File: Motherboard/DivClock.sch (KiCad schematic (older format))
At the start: 33 parts

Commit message: More work on Motherboard
Began work on PCB Routing
Began work on DMA
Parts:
- removed U?: 74AHC1G14, symbol 74xGxx:74AHC1G14
- added U13: 74LS14, symbol 74xx:74LS14
- added unit 7 of U16
- added U17: 74LS32, Housings_DIP:DIP-14_W7.62mm_Socket, symbol 74xx:74LS32
- added unit 5 of U18
- added unit 5 of U20
- added U21: 40106, Housings_DIP:DIP-40_W15.24mm_Socket, symbol 4xxx:40106
- R3, R4: renamed from R?; footprint (none) -> Resistors_THT:R_Axial_DIN0204_L3.6mm_D1.6mm_P5.08mm_Horizontal
- SW1: renamed from SW?; value SW_SPST -> TURBO; footprint (none) -> Pin_Headers:Pin_Header_Straight_1x02_Pitch2.00mm
- SW2: renamed from SW?; value SW_SPST -> FREEZE; footprint (none) -> Pin_Headers:Pin_Header_Straight_1x02_Pitch2.00mm
- U10, U11, U16, U18, U19, U20, U8, U9: renamed from U?; footprint (none) -> Housings_DIP:DIP-14_W7.62mm_Socket
- gave numbers to parts that had none: 11
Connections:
- wire segments 122 -> 128
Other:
- moved on the sheet: R3, R4

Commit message: Large sync
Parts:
- removed unit 1 of U18
- removed unit 1 of U20
- added unit 1 of U10
- U13: footprint (none) -> Housings_DIP:DIP-14_W7.62mm_Socket
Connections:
- net SYS_CLK: now also U19.9 (Q)
- net at U15.4 (Za), U16.3, U19.3 (C): now also U19.11 (C)
- net at U19.2 (D): now also U10.3; no longer U19.6 (~Q)
- net at U19.5 (Q): now also U19.12 (D); no longer U19.11 (C)
- net at U19.8 (~Q): now also U10.2; no longer U19.12 (D)
- new net: U10.1, U19.6 (~Q)
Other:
- moved on the sheet: U19B
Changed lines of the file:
@@
 L 74xx:74HC74 U19
 U 2 1 5BFDC06F
-P 8775 1225
-F 0 "U19" H 8925 1525 50  0000 C CNN
-F 1 "74HC74" H 9075 930 50  0000 C CNN
-F 2 "Housings_DIP:DIP-14_W7.62mm_Socket" H 8775 1225 50  0001 C CNN
-F 3 "" H 8775 1225 50  0001 C CNN
-	2    8775 1225
-	1    0    0    -1
-$EndComp
-$Comp
-L 4xxx:4081 U18
-U 1 1 5BFDE512
-P 9175 2425
-F 0 "U18" H 9175 2475 50  0000 C CNN
-F 1 "4081" H 9175 2375 50  0000 C CNN
-F 2 "Housings_DIP:DIP-14_W7.62mm_Socket" H 9175 2425 60  0001 C CNN
-F 3 "" H 9175 2425 60  0001 C CNN
-	1    9175 2425
-	1    0    0    -1
-$EndComp
-$Comp
-L 74xx:7402 U20
-U 1 1 5BFDF6A5
-P 10200 3200
-F 0 "U20" H 10200 3250 50  0000 C CNN
-F 1 "7402" H 10250 3150 50  0000 C CNN
-F 2 "Housings_DIP:DIP-14_W7.62mm_Socket" H 10200 3200 50  0001 C CNN
-F 3 "" H 10200 3200 50  0001 C CNN
-	1    10200 3200
-	0    1    1    0
+P 8750 2525
+F 0 "U19" H 8900 2825 50  0000 C CNN
+F 1 "74HC74" H 9050 2230 50  0000 C CNN
+F 2 "Housings_DIP:DIP-14_W7.62mm_Socket" H 8750 2525 50  0001 C CNN
+F 3 "" H 8750 2525 50  0001 C CNN
+	2    8750 2525
+	1    0    0    -1
 $EndComp
 Text Label 10200 3825 0    60   ~ 0
@@
 	3975 2475 5375 2475
 Wire Wire Line
-	9375 1900 8000 1900
-Wire Wire Line
-	8000 1900 8000 1125
-Wire Wire Line
 	6925 2525 6925 3250
 Wire Wire Line
@@
 	7875 2625 8025 2625
 Wire Wire Line
-	8025 2625 8025 2950
-Wire Wire Line
-	8025 2950 7150 2950
-Wire Wire Line
-	7150 2950 7150 2425
-Wire Wire Line
-	7150 2425 7275 2425
-Wire Wire Line
 	6925 2525 7275 2525
 Wire Wire Line
@@
 	-1   0    0    1
 $EndComp
-Wire Wire Line
-	7875 2425 8175 2425
-Wire Wire Line
-	8175 2425 8175 2325
-Connection ~ 8175 2325
-Wire Wire Line
-	8175 1225 8475 1225
-Wire Wire Line
-	8175 1225 8175 2325
-Wire Wire Line
-	8000 1125 8475 1125
-Wire Wire Line
-	9375 1325 9075 1325
-Wire Wire Line
-	9375 1325 9375 1900
-Wire Wire Line
-	9075 1125 10300 1125
-Wire Wire Line
-	8175 2325 8875 2325
-Wire Wire Line
-	8225 2525 8875 2525
-Wire Wire Line
-	9475 2425 10100 2425
-Wire Wire Line
-	10100 2425 10100 2900
-Wire Wire Line
-	10300 1125 10300 2900
-Wire Wire Line
-	10200 3500 10200 3850
 Wire Wire Line
 	9850 3850 9850 4000
@@
 F 0 "U13" V 4379 5805 50  0000 L CNN
 F 1 "74LS14" V 4470 5805 50  0000 L CNN
-F 2 "" H 4425 5625 50  0001 C CNN
+F 2 "Housings_DIP:DIP-14_W7.62mm_Socket" H 4425 5625 50  0001 C CNN
 F 3 "http://www.ti.com/lit/gpn/sn74LS14" H 4425 5625 50  0001 C CNN
 	1    4425 5625
 	0    1    1    0
 $EndComp
+Wire Wire Line
+	7875 2425 8450 2425
+Wire Wire Line
+	8450 2525 8225 2525
+$Comp
+L 4xxx:4081 U10
+U 1 1 5C493CC7
+P 7525 1800
+F 0 "U10" H 7525 1483 50  0000 C CNN
+F 1 "4081" H 7525 1574 50  0000 C CNN
+F 2 "Housings_DIP:DIP-14_W7.62mm_Socket" H 7525 1800 50  0001 C CNN
+F 3 "http://www.intersil.com/content/dam/Intersil/documents/cd40/cd4073bms-81bms-82bms.pdf" H 7525 1800 50  0001 C CNN
+	1    7525 1800
+	-1   0    0    1
+$EndComp
+Wire Wire Line
+	7225 1800 7225 2425
+Wire Wire Line
+	7225 2425 7275 2425
+Wire Wire Line
+	7825 1900 8025 1900
+Wire Wire Line
+	8025 1900 8025 2625
+Wire Wire Line
+	9050 2625 9125 2625
+Wire Wire Line
+	9125 2625 9125 1700
+Wire Wire Line
+	9125 1700 7825 1700
+Wire Wire Line
+	9050 2425 10200 2425
+Wire Wire Line
+	10200 2425 10200 3850
 $EndSCHEMATC

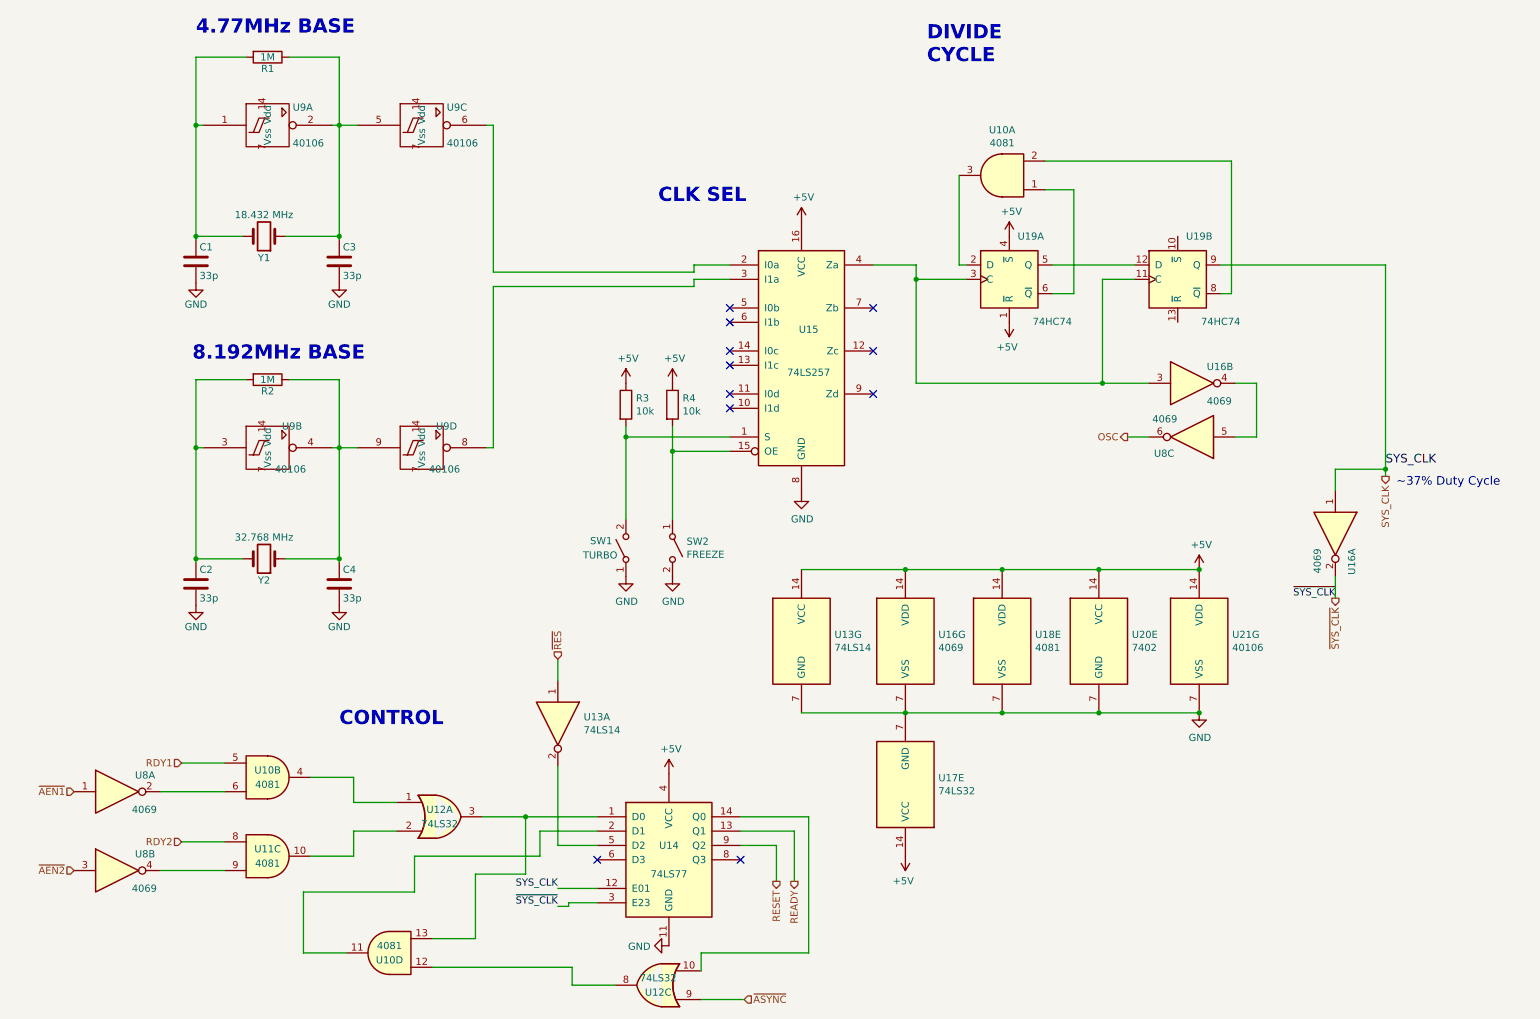
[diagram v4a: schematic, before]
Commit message: Work on motherboard  - Integrating glue logic into CPLD  - Began work on routing
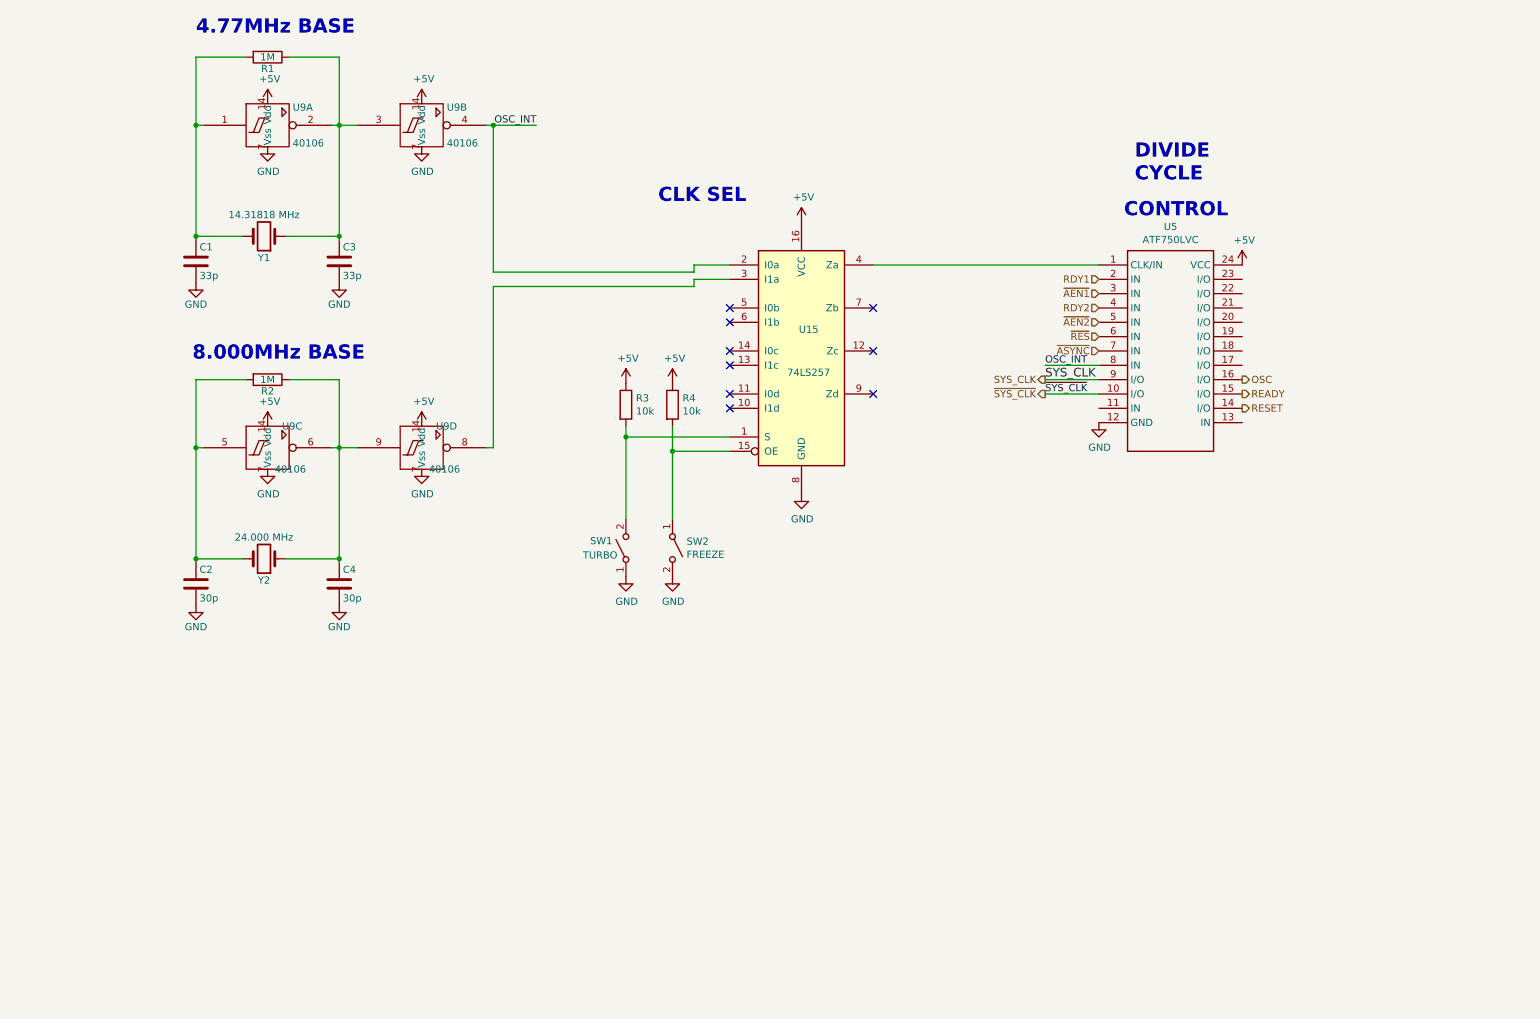
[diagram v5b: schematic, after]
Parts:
- removed U10, U11, U18: 4081, Housings_DIP:DIP-14_W7.62mm_Socket, symbol 4xxx:4081
- removed U12, U17: 74LS32, Housings_DIP:DIP-14_W7.62mm_Socket, symbol 74xx:74LS32
- removed U13: 74LS14, Housings_DIP:DIP-14_W7.62mm_Socket, symbol 74xx:74LS14
- removed U14: 74LS77, Housings_DIP:DIP-14_W7.62mm_Socket, symbol 74xx:74LS77
- removed U16, U8: 4069, Housings_DIP:DIP-14_W7.62mm_Socket, symbol 4xxx:4069
- removed U19: 74HC74, Housings_DIP:DIP-14_W7.62mm_Socket, symbol 74xx:74HC74
- removed U20: 7402, Housings_DIP:DIP-14_W7.62mm_Socket, symbol 74xx:7402
- removed U21: 40106, Housings_DIP:DIP-40_W15.24mm_Socket, symbol 4xxx:40106
- added U5: ATF750LVC, Housings_DIP:DIP-24_W7.62mm_Socket, symbol fdc:ATF750LVC
- C2, C4: value 33p -> 30p
- Y1: value 18.432 MHz -> 14.31818 MHz
- Y2: value 32.768 MHz -> 24.000 MHz
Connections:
- net +5V: now also U9.14 (Vdd), U9.14 (Vdd), U9.14 (Vdd), U9.14 (Vdd), U5.24 (VCC)
- net GND: now also U9.7 (Vss), U9.7 (Vss), U9.7 (Vss), U9.7 (Vss), U5.12 (GND)
- net OSC: now also U5.16 (I/O)
- net RDY1: now also U5.2 (IN)
- net RDY2: now also U5.4 (IN)
- net READY: now also U5.15 (I/O)
- net RESET: now also U5.14 (I/O)
- net SYS_CLK: now also U5.9 (I/O)
- net ~AEN1: now also U5.3 (IN)
- net ~AEN2: now also U5.5 (IN)
- net ~ASYNC: now also U5.7 (IN)
- net ~RES: now also U5.6 (IN)
- net ~SYS_CLK: now also U5.10 (I/O)
- net at C3.1, R1.1, U9.2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: now also U9.3; no longer U9.5
- net at C4.1, R2.1, U9.9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: now also U9.6; no longer U9.4
- net at C2.1, R2.2, Y2.2: now also U9.5; no longer U9.3
- net OSC_INT: now reaches U15.2 (I0a)
- net OSC_INT: now also U9.4, U5.8 (IN); no longer U9.6
- net at U15.4 (Za): now also U5.1 (CLK/IN)
- no-connect marks 11 -> 9
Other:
- note added: "8.000MHz BASE"
- note removed: "8.192MHz BASE"
- note removed: "~~37% Duty Cycle"

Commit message: from pc sync
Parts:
- U5: symbol fdc:ATF750LVC -> Motherboard-rescue:ATF750LVC-fdc
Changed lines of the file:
@@
 	4900 3625 4900 4200
 $Comp
-L fdc:ATF750LVC U5
+L Motherboard-rescue:ATF750LVC-fdc U5
 U 1 1 5C531418
 P 8700 3025
